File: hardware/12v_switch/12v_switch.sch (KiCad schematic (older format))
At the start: 59 parts, among them J1 Screw_Terminal_01x04, J2 Conn_01x06, J3 Conn_01x06, M1 SCREW_6-32_POWER, M19 SCREW_6-32_NORMAL, M2 SCREW_6-32_POWER, M20 SCREW_6-32_NORMAL, M21 SCREW_6-32_NORMAL, M22 SCREW_6-32_NORMAL, SW1 SW_Push, SW2 SW_Push, U1 DIRTBAG_DualChannel_PowerSwit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, U2 DIRTBAG_DualChannel_PowerSwit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, U3 TI_TPS25947A, U4 DIRTBAG_QUICKBUCK, U5 DIRTBAG_DualChannel_PowerSwit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, U6 DIRTBAG_DualChannel_PowerSwit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, U7 STM32F334K4Tx, U8 TI_TCAN334GDR, U9 SPARKFUN_COM-18357

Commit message: Relayed layout with integrated drivers.
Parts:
- removed C1, C4: SMD-CAP-1UF-0402, DBLS_Capacitor:C_0402_1005Metric, symbol DBLS_Capacitor:SMD-CAP-1UF-0402
- removed C2, C3: MURATA_GCM155R71H102KA37D, Capacitors_SMD:C_0402_NoSilk, symbol DBLS_Capacitor:MURATA_GCM155R71H102KA37D
- removed R1: VISHAYDALE_RCS0402470KJNED, Resistors_SMD:R_0402, symbol DBLS_Resistor:VISHAYDALE_RCS0402470KJNED
- removed R2: VISHAYDALE_CRCW040239K0FKEDHP, Resistors_SMD:R_0402, symbol DBLS_Resistor:VISHAYDALE_CRCW040239K0FKEDHP
- removed R3: VISHAYDALE_CRCW040243K0JNED, Resistors_SMD:R_0402, symbol DBLS_Resistor:VISHAYDALE_CRCW040243K0JNED
- removed R5: VISHAYDALE_CRCW0402620RJNED, Resistors_SMD:R_0402, symbol DBLS_Resistor:VISHAYDALE_CRCW0402620RJNED
- removed R6: VISHAYDALE_CRCW04021M00JNED, Resistors_SMD:R_0402, symbol DBLS_Resistor:VISHAYDALE_CRCW04021M00JNED
- removed SW1: SW_Push, symbol Switch:SW_Push
- removed TP8, TP9: DBLS_TESTPOINT_NORMAL, DBLS_Misc:DBLS_Testpoint_Normal, symbol DBLS_Misc:DBLS_TESTPOINT_NORMAL
- removed U1, U2, U5, U6: DIRTBAG_DualChannel_PowerSwitch, DBLS_Misc:DBLS_DualChannel_PowerSwitch, symbol DBLS_Device:DIRTBAG_DualChannel_PowerSwitch
- removed U3: TI_TPS25947A, DBLS_Resistor:R_0603_1608Metric, symbol DBLS_Device:TI_TPS25947A
- added F1: LITTLEFUSE_RGEF700-2, DBLS_Misc:LITTLEFUSE_RGEF, symbol DBLS_Misc:LITTLEFUSE_RGEF700-2
- J2: footprint SparkFun-Connectors:SCREWTERMINAL-3.5MM-6 -> Pin_Headers:Pin_Header_Straight_1x06_Pitch2.54mm
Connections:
- net labels removed: FUSE_PGOOD, FUSE_RESET
- wire segments 247 -> 153
- no-connect marks 25 -> 9
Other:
- note added: "9A TRACE"
- note added: "INPUT POWER / FUSE"
- note removed: "3.3nF\n"
- note removed: "39k\n"
- note removed: "43k"
- note removed: "550Ohm\n\n"
- note removed: "6A TRACE"
- note removed: "E-FUSE"
- note removed: "NOTE: The Switches have the 6-32 mounting spots"
- note removed: "Vov = 15.4V"
- note removed: "Vuv = 8.1V"
- moved on the sheet: JP1, JP2, JP3, JP4, M1, M19, M2, M20, M21, M22, TP1, TP2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

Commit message: Added fp lib and netlist. Saving before removing mcu.
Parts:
- removed U7: STM32F334K4Tx, Package_QFP:LQFP-32_7x7mm_P0.8mm, symbol MCU_ST_STM32F3:STM32F334K4Tx
- added U?: STMICRO_STM32F334K6T6, Housings_QFP:LQFP-32_7x7mm_Pitch0.8mm, symbol DBLS_MCU:STMICRO_STM32F334K6T6
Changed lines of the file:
@@
-$EndComp
-$Comp
-L MCU_ST_STM32F3:STM32F334K4Tx U7
-U 1 1 61629CC5
-P 8100 4000
-F 0 "U7" H 7600 4850 50  0000 L CNN
-F 1 "STM32F334K4Tx" H 8300 4850 50  0000 L CNN
-F 2 "Package_QFP:LQFP-32_7x7mm_P0.8mm" H 7600 3100 50  0001 R CNN
-F 3 "http://www.st.com/st-web-ui/static/active/en/resource/technical/document/datasheet/DM00097745.pdf" H 8100 4000 50  0001 C CNN
-	1    8100 4000
-	1    0    0    -1
 $EndComp
 $Comp
@@
 Wire Wire Line
 	3150 6450 3450 6450
+$Comp
+L DBLS_MCU:STMICRO_STM32F334K6T6 U?
+U 1 1 61A1ACC3
+P 8100 4000
+F 0 "U?" H 7600 4850 50  0000 L CNN
+F 1 "STMICRO_STM32F334K6T6" H 8300 4850 50  0001 L CNN
+F 2 "Housings_QFP:LQFP-32_7x7mm_Pitch0.8mm" H 7600 3100 50  0001 R CNN
+F 3 "http://www.st.com/st-web-ui/static/active/en/resource/technical/document/datasheet/DM00097745.pdf" H 8100 4000 50  0001 C CNN
+F 4 "STM32F334K6T6" H 8100 4000 40  0000 C CNN "mfg_pn"
+F 5 "STMicroelectronics" H 8100 4000 50  0001 C CNN "mfg"
+F 6 "digikey" H 8100 4000 50  0001 C CNN "vendor"
+F 7 "497-14952-5-ND" H 8100 4000 50  0001 C CNN "vendor_pn"
+F 8 "YES" H 8100 4000 30  0001 C CNN "place"
+F 9 "IC MCU 32BIT 32KB FLASH 32LQFP" H 8100 4000 50  0001 C CNN "description"
+	1    8100 4000
+	1    0    0    -1
+$EndComp
 $EndSCHEMATC

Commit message: First draft layout with 4 switches + buck
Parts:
- removed C5, C7, C8: MURATA_GCM155R71C104KA55J, Capacitors_SMD:C_0402, symbol DBLS_Capacitor:MURATA_GCM155R71C104KA55J
- removed D1: INOLUX_IN-S63BTR, LEDs:LED_0603, symbol DBLS_Diode:INOLUX_IN-S63BTR
- removed J1: Screw_Terminal_01x04, Connectors:bornier4, symbol Connector:Screw_Terminal_01x04
- removed J2, J3: Conn_01x06, Pin_Headers:Pin_Header_Straight_1x06_Pitch2.54mm, symbol Connector_Generic:Conn_01x06
- removed JP3, JP4, JP5: PAD_JUMPER_2PIN_NC, DBLS_Misc:PAD_JUMPER_2PIN_NC, symbol DBLS_Misc:PAD_JUMPER_2PIN_NC
- removed R11, R12: VISHAYDALE_CRCW040233R0JNEDC, Resistors_SMD:R_0402, symbol DBLS_Resistor:VISHAYDALE_CRCW040233R0JNEDC
- removed R13: VISHAYDALE_RCS0805120RJNEA, Resistors_SMD:R_0805, symbol DBLS_Resistor:VISHAYDALE_RCS0805120RJNEA
- removed R14: VISHAYDALE_CRCW0402620RJNED, Resistors_SMD:R_0402, symbol DBLS_Resistor:VISHAYDALE_CRCW0402620RJNED
- removed R4, R8: VISHAYDALE_CRCW040210K0FKED, Resistors_SMD:R_0402, symbol DBLS_Resistor:VISHAYDALE_CRCW040210K0FKED
- removed R7, R9: VISHAYDALE_CRCW0402100KJNEDC, Resistors_SMD:R_0402, symbol DBLS_Resistor:VISHAYDALE_CRCW0402100KJNEDC
- removed SW2: SW_Push, symbol Switch:SW_Push
- removed TP1, TP10, TP11, TP12, TP3, TP4: DBLS_TESTPOINT_NORMAL, DBLS_Misc:DBLS_Testpoint_Normal, symbol DBLS_Misc:DBLS_TESTPOINT_NORMAL
- removed U4: DIRTBAG_QUICKBUCK, DBLS_Misc:DBLS_QuickBuck, symbol DBLS_Device:DIRTBAG_QUICKBUCK
- removed U8: TI_TCAN334GDR, Housings_SOIC:SOIC-8_3.9x4.9mm_Pitch1.27mm, symbol DBLS_Device:TI_TCAN334GDR
- removed U9: SPARKFUN_COM-18357, DBLS_Misc:SPARKFUN_BABYBUCK, symbol DBLS_Device:SPARKFUN_COM-18357
- removed U?: STMICRO_STM32F334K6T6, Housings_QFP:LQFP-32_7x7mm_Pitch0.8mm, symbol DBLS_MCU:STMICRO_STM32F334K6T6
- added C1, C2: SMD-CAP-1UF-0402, DBLS_Capacitor:C_0402_1005Metric, symbol DBLS_Capacitor:SMD-CAP-1UF-0402
- added C10: VISHAY_593D107X0020E2TE3, DBLS_Capacitor:C_2917, symbol DBLS_Capacitor:VISHAY_593D107X0020E2TE3
- added C3, C4: MURATA_GRM155R71H104ME14J, Capacitors_SMD:C_0402, symbol DBLS_Capacitor:MURATA_GRM155R71H104ME14J
- added C7: MURATA_GRM31CC81E226KE11L, Capacitors_SMD:C_1206, symbol DBLS_Capacitor:MURATA_GRM31CC81E226KE11L
- added C8: MURATA_GRT31CR61H106KE01L, Capacitors_SMD:C_1206, symbol DBLS_Capacitor:MURATA_GRT31CR61H106KE01L
- added C9: MURATA_GCM155R71E103KA37D, Capacitors_SMD:C_0402, symbol DBLS_Capacitor:MURATA_GCM155R71E103KA37D
- added D2: VISHAY_SSA33L-E3_61T, Diodes_SMD:D_SMA, symbol DBLS_Diode:VISHAY_SSA33L-E3_61T
- added F2, F3, F6, F7: LITTLEFUSE_RGEF300-2, DBLS_Misc:LITTLEFUSE_RGEF, symbol DBLS_Misc:LITTLEFUSE_RGEF300-2
- added J1: MOLEX_0530470810, Connectors_Molex:Molex_PicoBlade_53047-0810_08x1.25mm_Straight, symbol DBLS_Connectors:MOLEX_0530470810
- added JP2: PAD_JUMPER_2PIN_NC, DBLS_Misc:PAD_JUMPER_2PIN_NC, symbol DBLS_Misc:PAD_JUMPER_2PIN_NC
- added L2: PANASONIC_ETQ-P3M100KVN, DBLS_Inductor:L_6.4x6.0_H3, symbol DBLS_Inductor:PANASONIC_ETQ-P3M100KVN
- added M11, M12, M13, M14, M3, M4, M5, M6: SCREW_6-32_POWER, DBLS_Mechanical:SCREW_6-32_POWER, symbol DBLS_Mechanical:SCREW_6-32_POWER
- added Q1, Q2, Q3, Q4: INFINEON_IRF7470TRPBF, Housings_SOIC:SOIC-8_3.9x4.9mm_Pitch1.27mm, symbol DBLS_Transistor:INFINEON_IRF7470TRPBF
- added R6: VISHAYDALE_CRCW04020000Z0EDHP, Resistors_SMD:R_0402, symbol DBLS_Resistor:VISHAYDALE_CRCW04020000Z0EDHP
- added R7: VISHAYDALE_CRCW04025K60JNED, Resistors_SMD:R_0402, symbol DBLS_Resistor:VISHAYDALE_CRCW04025K60JNED
- added R8: VISHAYDALE_CRCW04022K00JNEDC, Resistors_SMD:R_0402, symbol DBLS_Resistor:VISHAYDALE_CRCW04022K00JNEDC
- added U1, U2: TI_LM5111-1MX_NOPB, Housings_SOIC:SOIC-8_3.9x4.9mm_Pitch1.27mm, symbol DBLS_Device:TI_LM5111-1MX_NOPB
- added U3: TI_LM22680QMRE-ADJ, DBLS_SOIC:SOIC-8-1EP_3.9x4.9mm_Pitch1.27mm_ALT, symbol DBLS_Regulator:TI_LM22680QMRE-ADJ
- renumbered JP2 to JP3, TP2 to TP1, TP5 to TP2, TP6 to TP3, TP7 to TP4
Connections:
- net labels added: VBUS
- net labels removed: +3.3V, BOOT0, CAN1_H, CAN1_L, CAN_FAULT, CAN_RX, CAN_STNDBY, CAN_TX, EXTRA_IO1, EXTRA_IO2, EXTRA_IO3, LED, MCU_RX_DBG_TX, MCU_TX_DBG_RX, NRST, PWM5, PWM6, PWM7, PWM8, SWCLK, SWDIO, SWO, UART_RX, UART_TX
- wire segments 153 -> 123
- no-connect marks 9 -> 4
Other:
- note added: "5V POWER"
- note added: "5V/12V BUS SELECT"
- note added: "CONTROLLER INPUTS"
- note removed: "3.3V Regulator"
- note removed: "5V / 2A Power Supply"
- note removed: "AN2606: Pull-ups may not be required."
- note removed: "CAN"
- note removed: "DEBUG UART"
- note removed: "OSC"
- note removed: "Pull Boot0 High to enter bootloader"
- note removed: "ST_LINK Connector"
- note removed: "TODO: Add battery voltage monitor"
- moved on the sheet: JP1, JP3, M19, M20, M21, M22, TP1, TP2, TP3, TP4

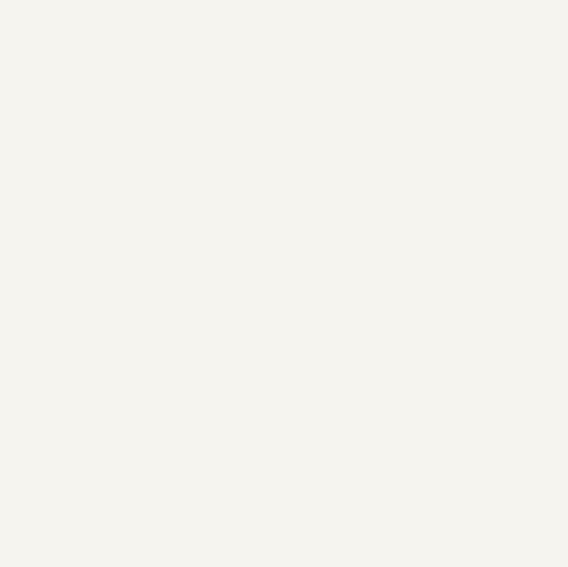
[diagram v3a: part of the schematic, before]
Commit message: fixed designators. Added logo and labels
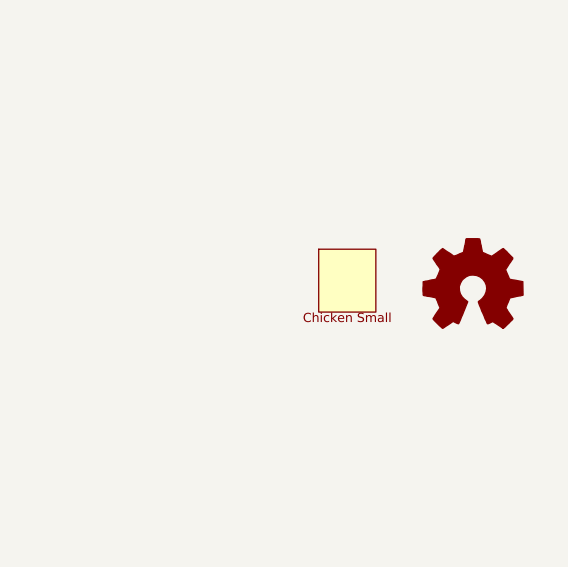
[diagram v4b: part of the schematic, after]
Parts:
- added LOGO1: DBLS_Chicken_Small, DBLS_LOGO:Rooster_4mmx4mm, symbol DBLS_Logo:DBLS_Chicken_Small
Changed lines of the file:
@@
 Wire Wire Line
 	9350 1500 9850 1500
+$Comp
+L Graphic:Logo_Open_Hardware_Small #LOGO1
+U 1 1 617DAD86
+P 10600 5950
+F 0 "#LOGO1" H 10600 6225 50  0001 C CNN
+F 1 "Logo_Open_Hardware_Small" H 10600 5725 50  0001 C CNN
+F 2 "" H 10600 5950 50  0001 C CNN
+F 3 "~" H 10600 5950 50  0001 C CNN
+	1    10600 5950
+	1    0    0    -1
+$EndComp
+$Comp
+L DBLS_Logo:DBLS_Chicken_Small LOGO1
+U 1 1 617DB4DD
+P 10050 5900
+F 0 "LOGO1" H 10050 5900 50  0001 C CNN
+F 1 "DBLS_Chicken_Small" H 10050 5900 50  0001 C CNN
+F 2 "DBLS_LOGO:Rooster_4mmx4mm" H 10080 6050 20  0001 C CNN
+F 3 "" H 10050 5900 50  0001 C CNN
+F 4 "DNI" H 10050 5900 50  0001 C CNN "place"
+	1    10050 5900
+	1    0    0    -1
+$EndComp
 $EndSCHEMATC
